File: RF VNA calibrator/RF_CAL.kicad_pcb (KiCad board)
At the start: 2 copper layers, 17 x 9.5 mm, 7 parts

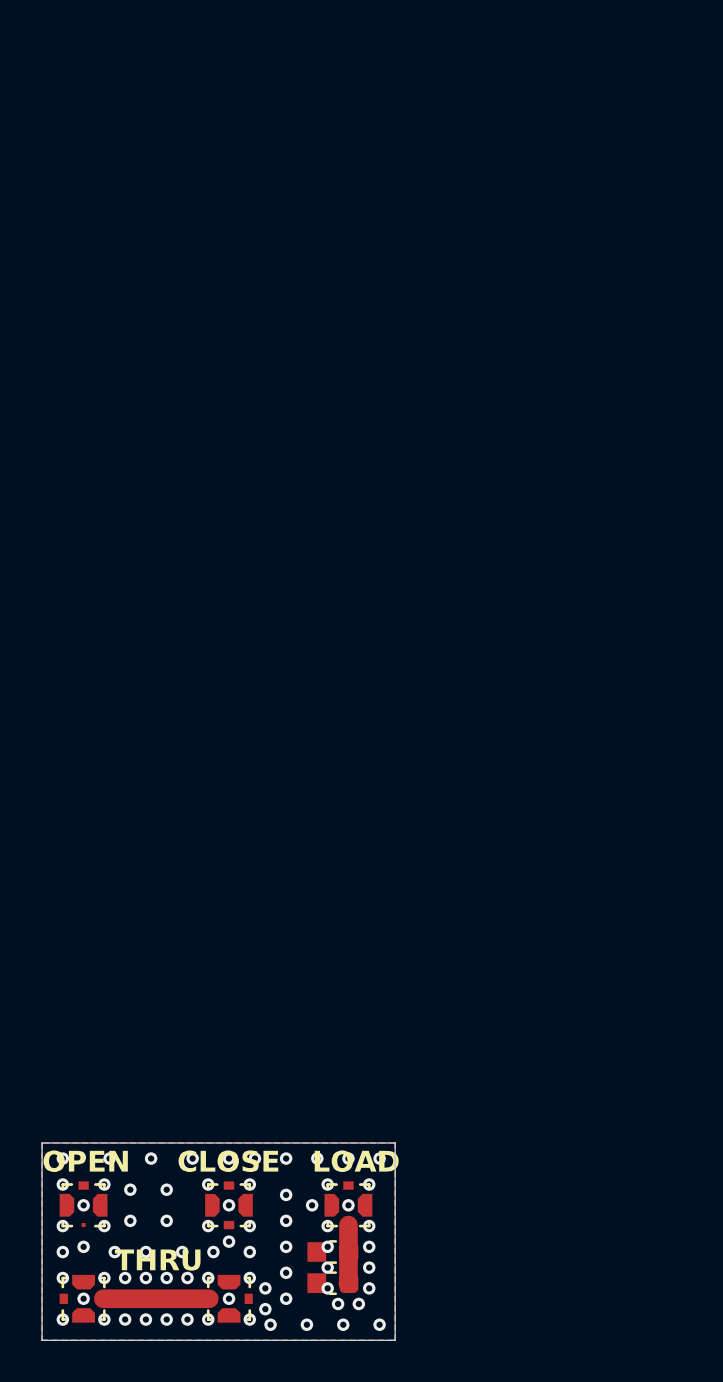
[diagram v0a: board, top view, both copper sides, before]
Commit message: Cleanup & standardize schematic & PCB
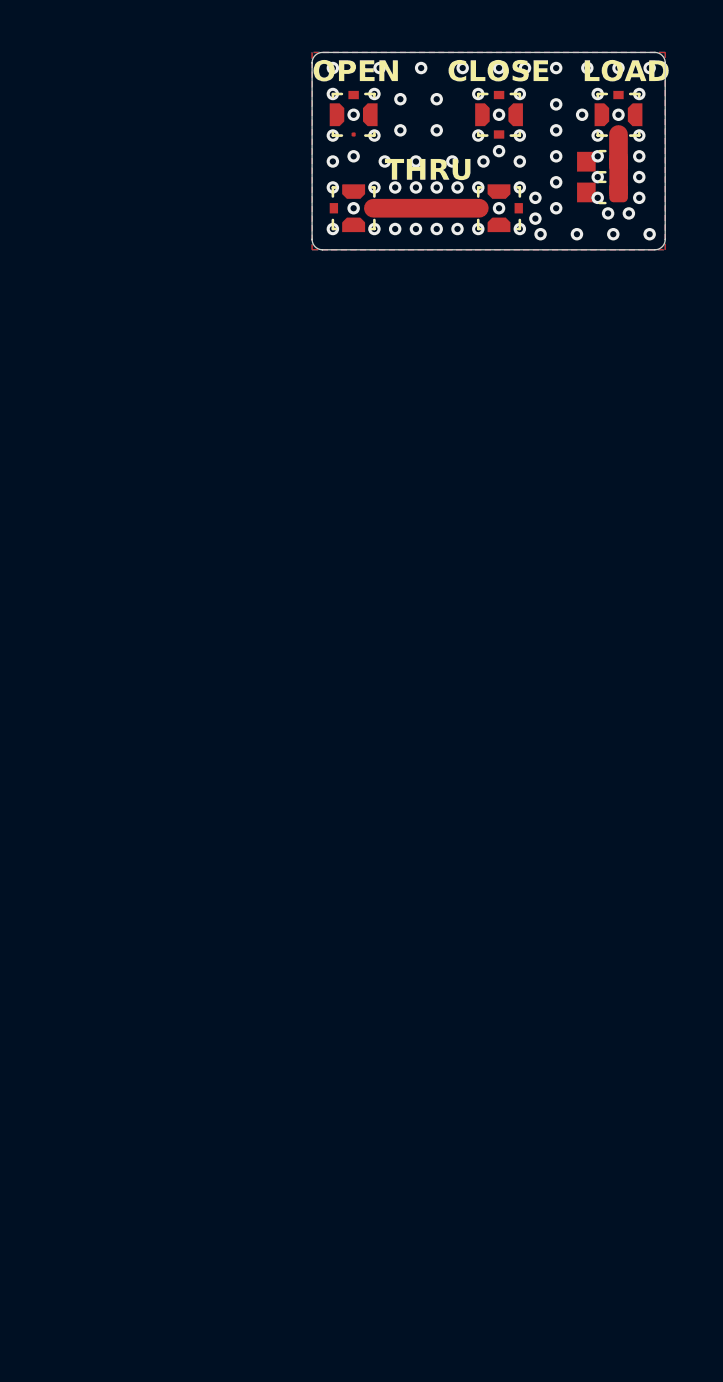
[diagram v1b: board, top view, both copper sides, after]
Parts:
- moved R2 54.1 mm to (106.0, 82.2)
- moved TP1 54.1 mm to (101.0, 78.5)
- moved TP2 54.1 mm to (94.0, 78.5)
- moved TP3 54.1 mm to (106.8, 78.5)
- moved TP4 54.1 mm to (101.0, 83.0)
- moved TP5 54.1 mm to (94.0, 83.0)
- moved R1 54.1 mm to (106.0, 80.8)
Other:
- outline, holes or cut-outs redrawn
- board text added: "V1.0"
- board text added: "VNA calibration board"

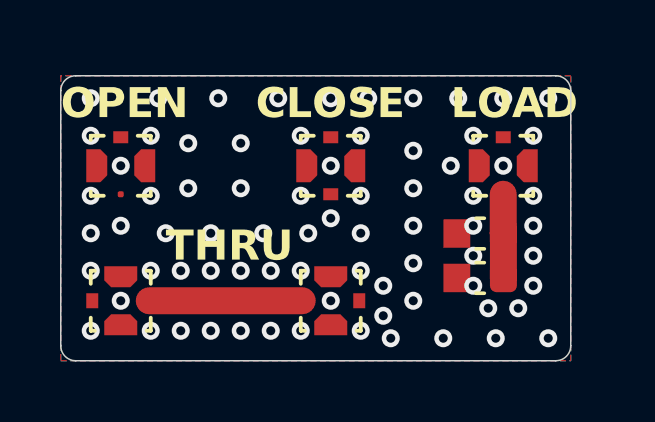
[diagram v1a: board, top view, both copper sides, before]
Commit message: Finish VNA calibration board, production files
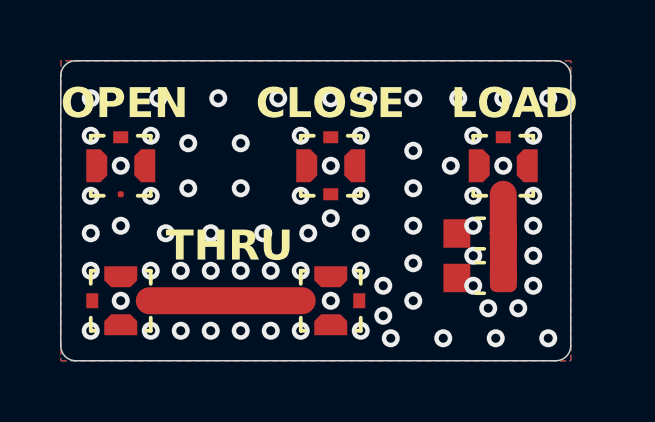
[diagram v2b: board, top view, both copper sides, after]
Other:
- board size 17 x 9.5 mm -> 17 x 10 mm
